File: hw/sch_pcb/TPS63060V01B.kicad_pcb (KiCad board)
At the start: 2 copper layers, 30 x 40.1 mm, 27 parts, among them P1 1,1A, X1 SROUB3M, X2 SROUB3M, X3 SROUB3M, X4 SROUB3M, X5 TPS63060, X9 APX809

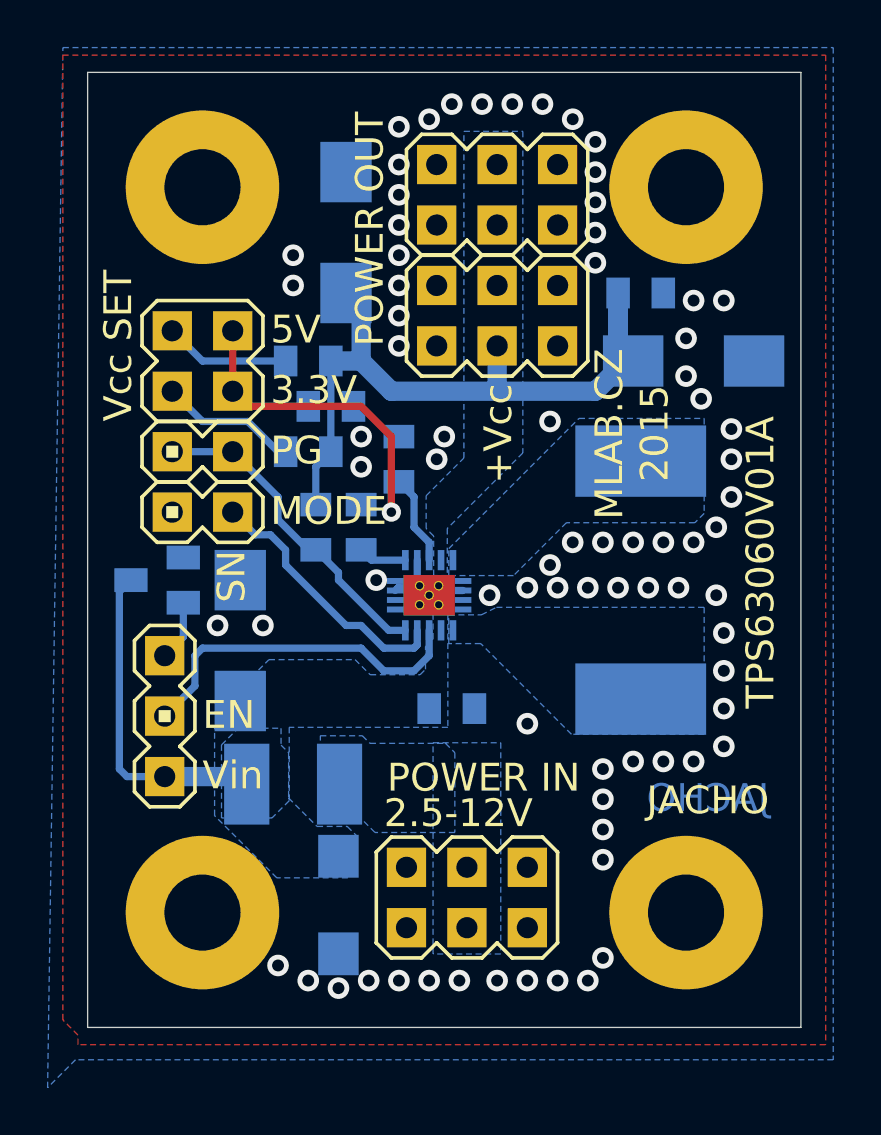
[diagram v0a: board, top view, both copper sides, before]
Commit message: urpava shema a pouzder kvuli prechodu z eagle
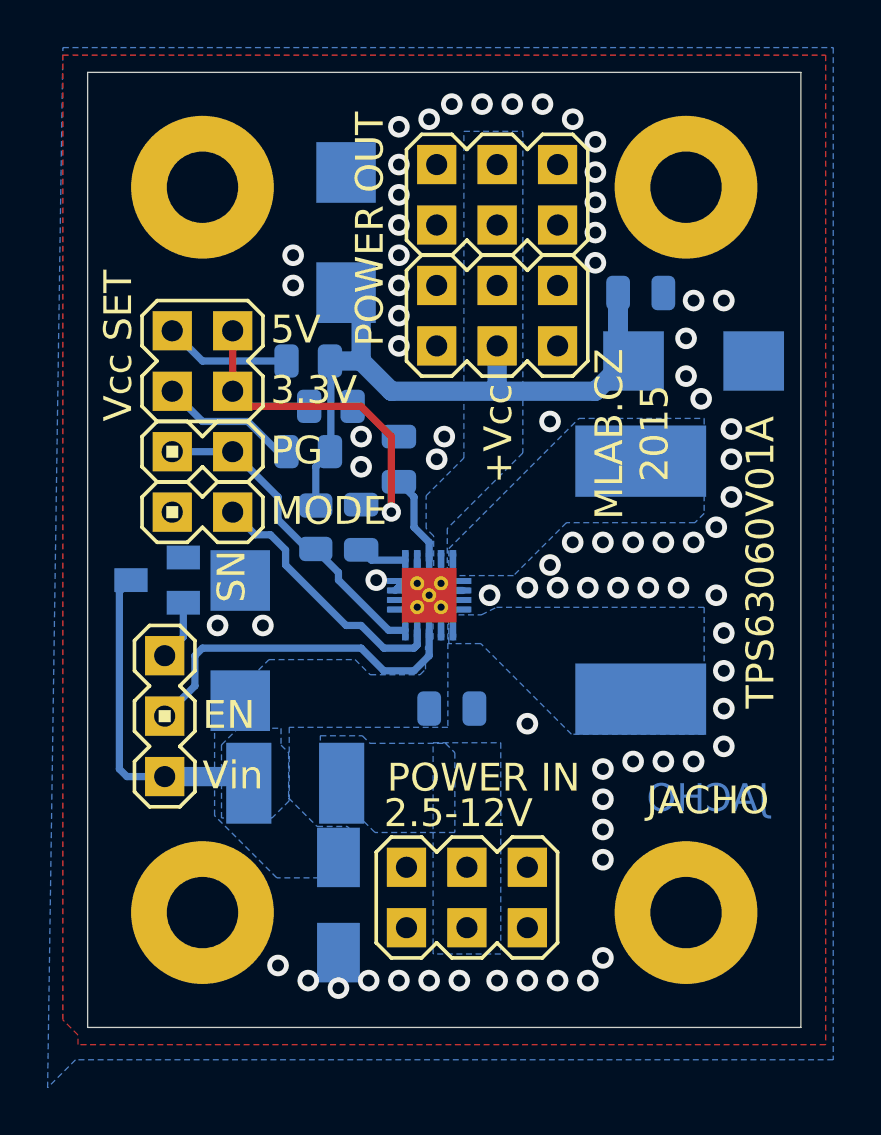
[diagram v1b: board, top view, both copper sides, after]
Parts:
- C1, C16, C2, C5: footprint untitled:C0805 -> Capacitor_SMD:C_0805_2012Metric
- C20: footprint untitled:C -> Mlab_C:TantalC_SizeC_Reflow
- C3, C6: value 47u -> 47uF; footprint untitled:C -> Mlab_C:TantalC_SizeC_Reflow
- D1: footprint untitled:SMA -> Diode_SMD:D_SMA
- L1: footprint untitled:DE1205-10 -> Mlab_L:DE1205-10
- P1: footprint untitled:1812 -> Mlab_F:1812
- R2, R3, R4, R5: footprint untitled:0805 -> Resistor_SMD:R_0805_2012Metric
- SV1: value (none) -> MA03-1
- SV2, SV3, SV5: value (none) -> MA03-2
- SV4: value (none) -> MA02-3
- X1, X2, X3, X4: footprint untitled:SROUB3M -> Mlab_Mechanical:MountingHole_3mm
- X5: footprint untitled:SON10 -> Package_SON:Texas_S-PWSON-N10_ThermalVias
- moved P1 0.10 mm to (142.2, 114.8)
- turned C20 to 90 degrees
- turned C3 to 90 degrees
- turned C6 to 0 degrees
- turned D1 to -90 degrees
- turned L1 to -90 degrees
- turned X5 to 90 degrees
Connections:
- C16 pad 2: +BAT2 -> Net-(C20-Pad1)
- C2 pad 2: N$8 -> Net-(C3-Pad1)
- P1 pad 2: +BAT2 -> Net-(C20-Pad1)
- R3 pad 2: N$8 -> Net-(C3-Pad1)
- R4 pad 2: N$8 -> Net-(C3-Pad1)
- R5 pad 2: N$8 -> Net-(C3-Pad1)
- SV1 pad 3: +BAT2 -> Net-(C20-Pad1)
- SV2 pad 3: N$8 -> Net-(C3-Pad1)
- SV2 pad 4: N$8 -> Net-(C3-Pad1)
- SV5 pad 3: N$8 -> Net-(C3-Pad1)
- SV5 pad 4: N$8 -> Net-(C3-Pad1)
- X5 pad 1: N$15 -> Net-(X5-Pad1)
- X5 pad 10: N$16 -> Net-(X5-Pad10)
- X5 pad 2: +BAT2 -> Net-(C20-Pad1)
- X5 pad 9: N$8 -> Net-(C3-Pad1)
- X9 pad 3: +BAT2 -> Net-(C20-Pad1)
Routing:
- net Net-(C3-Pad1): track 0.00 -> 30.6 mm
- net N$8: track 30.6 -> 0.00 mm
- net +BAT2: track 13.8 -> 0.00 mm
- net Net-(C20-Pad1): track 0.00 -> 13.3 mm
- net Net-(X5-Pad10): vias 0 -> 3
- net Net-(X5-Pad1): vias 0 -> 4
- net GND: vias 76 -> 69
- added copper zone on B.Cu, net Net-(C20-Pad1)
- added copper zone on B.Cu, net Net-(C3-Pad1)
- added copper zone on B.Cu, net Net-(X5-Pad1)
- added copper zone on B.Cu, net Net-(X5-Pad10)
- removed copper zone on B.Cu, net +BAT2
- removed copper zone on B.Cu, net N$15
- removed copper zone on B.Cu, net N$16
- removed copper zone on B.Cu, net N$8
